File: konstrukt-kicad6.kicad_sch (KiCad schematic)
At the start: 0 parts

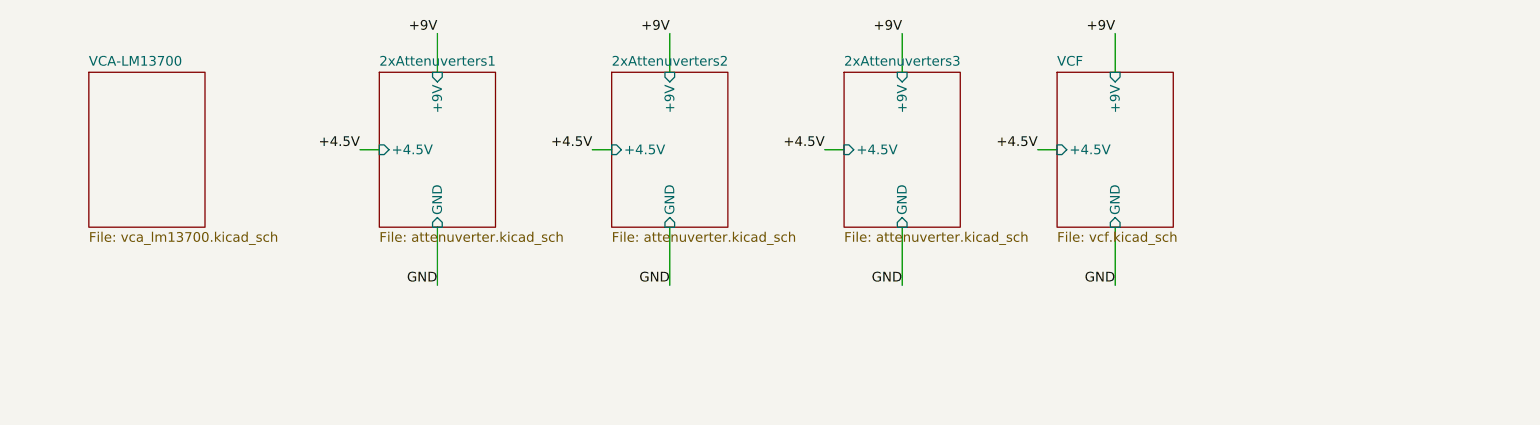
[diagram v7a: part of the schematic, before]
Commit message: VCF layout done, vca capture
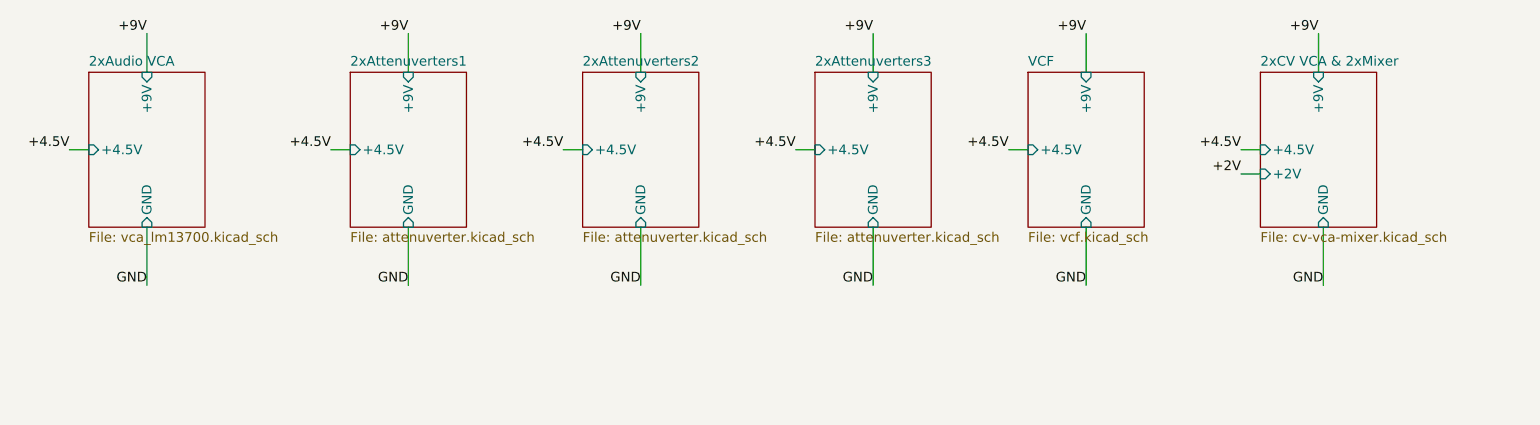
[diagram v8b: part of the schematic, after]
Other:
- sheet VCA-LM13700 renamed 2xAudio VCA
- added sheet 2xCV VCA & 2xMixer (cv-vca-mixer.kicad_sch)
- sheet 2xAudio VCA ports: added +4.5V, +9V, GND; removed none
